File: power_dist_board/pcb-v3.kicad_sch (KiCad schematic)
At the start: 9 parts, among them J1 Screw_Terminal_01x02, J2 Conn_01x07_Socket, J3 Screw_Terminal_01x02, J4 Screw_Terminal_01x02, J5 Conn_02x20_Odd_Even

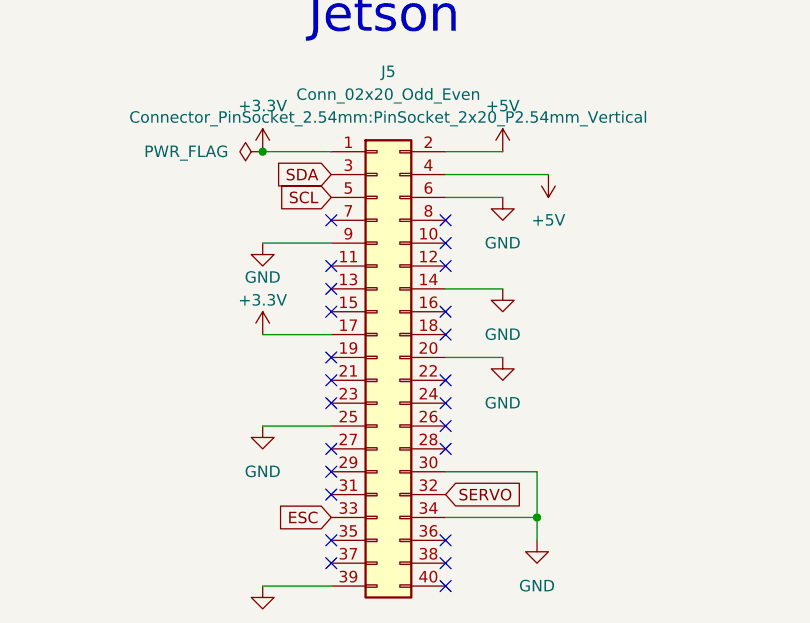
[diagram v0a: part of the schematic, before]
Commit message: Remap Jetson pins and update labels
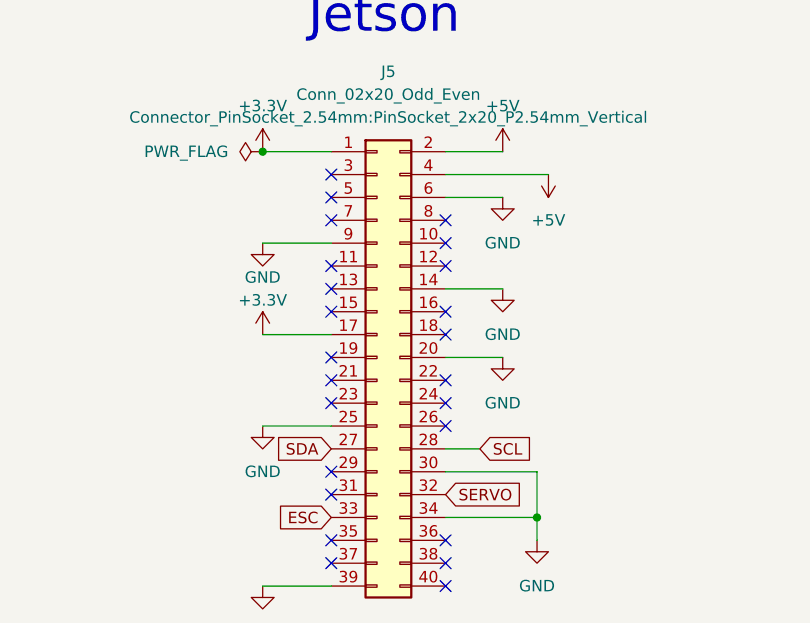
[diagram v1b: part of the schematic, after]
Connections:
- net SCL: now also J5.28 (Pin_28); no longer J5.5 (Pin_5)
- net SDA: now also J5.27 (Pin_27); no longer J5.3 (Pin_3)
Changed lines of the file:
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@@
 	)
 	(no_connect
-		(at 121.92 87.63)
+		(at 109.22 59.69)
 	)
 	(no_connect
@@
 	)
 	(no_connect
-		(at 109.22 87.63)
+		(at 109.22 57.15)
 	)
 	(no_connect
@@
 		(pts
 			(xy 46.99 143.51) (xy 46.99 138.43)
+		)
+		(stroke
+			(width 0)
+			(type default)
+		)
+	)
+	(wire
+		(pts
+			(xy 121.92 87.63) (xy 125.73 87.63)
 		)
 		(stroke
@@
 	(global_label "SDA"
 		(shape input)
-		(at 109.22 57.15 180)
+		(at 109.22 87.63 180)
 		(fields_autoplaced yes)
 		(effects
@@
 		)
 		(property "Intersheetrefs" "${INTERSHEET_REFS}"
-			(at 102.6667 57.15 0)
+			(at 102.6667 87.63 0)
 			(effects
 				(font
@@
 	(global_label "SCL"
 		(shape input)
-		(at 109.22 59.69 180)
-		(fields_autoplaced yes)
-		(effects
-			(font
-				(size 1.27 1.27)
-			)
-			(justify right)
-		)
-		(property "Intersheetrefs" "${INTERSHEET_REFS}"
-			(at 102.7272 59.69 0)
-			(effects
-				(font
-					(size 1.27 1.27)
-				)
-				(justify right)
-				(hide yes)
-			)
+		(at 125.73 87.63 0)
+		(fields_autoplaced yes)
+		(effects
+			(font
+				(size 1.27 1.27)
+			)
+			(justify left)
+		)
+		(property "Intersheetrefs" "${INTERSHEET_REFS}"
+			(at 132.2228 87.63 0)
+			(effects
+				(font
+					(size 1.27 1.27)
+				)
+				(justify left)
+				(hide yes)
+			)
